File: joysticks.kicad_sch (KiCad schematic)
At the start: 20 parts, among them IC14 74HCT574, IC15 4HCT574

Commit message: prepare for fabrication
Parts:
- C104, C96: LCSC (none) -> C344201; LCSC Part (none) -> C344201
- IC14: LCSC (none) -> C6001; LCSC Part (none) -> C6001
- IC15: value 4HCT574 -> 74HCT574; LCSC (none) -> C6001; LCSC Part (none) -> C6001
- R100, R101, R106, R107, R108, R109, R98, R99: LCSC (none) -> C149504; LCSC Part (none) -> C149504
- R111, R112: LCSC (none) -> C2907326; LCSC Part (none) -> C2907326
- R225, R226: LCSC (none) -> C17630; LCSC Part (none) -> C17630
- RP1: value 10K -> 10Kx8; LCSC (none) -> C1738939; LCSC Part (none) -> C1738939
- RP10: value 4K7 -> 4K7x8; LCSC (none) -> C1739872; LCSC Part (none) -> C1739872

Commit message: move RP11 inline instead of pullup
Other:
- moved on the sheet: RP1A, RP1G, RP1H, RP1I, RP1J
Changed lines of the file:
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@@
 		(lib_name "R_Network15_Split_1")
 		(lib_id "Acorn:R_Network15_Split")
-		(at 124.46 3.81 0)
+		(at 271.78 19.05 0)
 		(unit 1)
 		(exclude_from_sim no)
@@
 		(fields_autoplaced yes)
 		(property "Reference" "RP1"
-			(at 127 3.1749 0)
+			(at 274.32 18.4149 0)
 			(effects
 				(font
@@
 		)
 		(property "Value" "10Kx8"
-			(at 127 5.08 0)
+			(at 274.32 20.32 0)
 			(effects
 				(font
@@
 		)
 		(property "Footprint" "Package_SO:SOIC-16W_5.3x10.2mm_P1.27mm"
-			(at 124.46 3.81 0)
+			(at 271.78 19.05 0)
 			(effects
 				(font
@@
 		)
 		(property "Datasheet" ""
-			(at 124.46 3.81 0)
+			(at 271.78 19.05 0)
 			(effects
 				(font
@@
 		)
 		(property "Description" ""
-			(at 124.46 3.81 0)
+			(at 271.78 19.05 0)
 			(effects
 				(font
@@
 		)
 		(property "LCSC" "C1738939"
-			(at 124.46 3.81 0)
+			(at 271.78 19.05 0)
 			(effects
 				(font
@@
 		)
 		(property "LCSC Part" "C1738939"
-			(at 124.46 3.81 0)
+			(at 271.78 19.05 0)
 			(effects
 				(font
@@
 		(lib_name "R_Network15_Split_3")
 		(lib_id "Acorn:R_Network15_Split")
-		(at 130.81 3.81 0)
+		(at 271.78 26.67 0)
 		(unit 7)
 		(exclude_from_sim no)
@@
 		(fields_autoplaced yes)
 		(property "Reference" "RP1"
-			(at 133.35 3.1749 0)
+			(at 274.32 26.0349 0)
 			(effects
 				(font
@@
 		)
 		(property "Value" "10Kx8"
-			(at 133.35 5.08 0)
+			(at 274.32 27.94 0)
 			(effects
 				(font
@@
 		)
 		(property "Footprint" "Package_SO:SOIC-16W_5.3x10.2mm_P1.27mm"
-			(at 130.81 3.81 0)
+			(at 271.78 26.67 0)
 			(effects
 				(font
@@
 		)
 		(property "Datasheet" ""
-			(at 130.81 3.81 0)
+			(at 271.78 26.67 0)
 			(effects
 				(font
@@
 		)
 		(property "Description" ""
-			(at 130.81 3.81 0)
+			(at 271.78 26.67 0)
 			(effects
 				(font
@@
 		)
 		(property "LCSC" "C1738939"
-			(at 130.81 3.81 0)
+			(at 271.78 26.67 0)
 			(effects
 				(font
@@
 		)
 		(property "LCSC Part" "C1738939"
-			(at 130.81 3.81 0)
+			(at 271.78 26.67 0)
 			(effects
 				(font
@@
 		(lib_name "R_Network15_Split_2")
 		(lib_id "Acorn:R_Network15_Split")
-		(at 135.89 3.81 0)
+		(at 271.78 34.29 0)
 		(unit 8)
 		(exclude_from_sim no)
@@
 		(fields_autoplaced yes)
 		(property "Reference" "RP1"
-			(at 138.43 3.1749 0)
+			(at 274.32 33.6549 0)
 			(effects
 				(font
@@
 		)
 		(property "Value" "10Kx8"
-			(at 138.43 5.08 0)
+			(at 274.32 35.56 0)
 			(effects
 				(font
@@
 		)
 		(property "Footprint" "Package_SO:SOIC-16W_5.3x10.2mm_P1.27mm"
-			(at 135.89 3.81 0)
+			(at 271.78 34.29 0)
 			(effects
 				(font
@@
 		)
 		(property "Datasheet" ""
-			(at 135.89 3.81 0)
+			(at 271.78 34.29 0)
 			(effects
 				(font
@@
 		)
 		(property "Description" ""
-			(at 135.89 3.81 0)
+			(at 271.78 34.29 0)
 			(effects
 				(font
@@
 		)
 		(property "LCSC" "C1738939"
-			(at 135.89 3.81 0)
+			(at 271.78 34.29 0)
 			(effects
 				(font
@@
 		)
 		(property "LCSC Part" "C1738939"
-			(at 135.89 3.81 0)
+			(at 271.78 34.29 0)
 			(effects
 				(font
@@
 		(lib_name "R_Network15_Split_5")
 		(lib_id "Acorn:R_Network15_Split")
-		(at 142.24 3.81 0)
+		(at 271.78 41.91 0)
 		(unit 9)
 		(exclude_from_sim no)
@@
 		(fields_autoplaced yes)
 		(property "Reference" "RP1"
-			(at 144.78 3.1749 0)
+			(at 274.32 41.2749 0)
 			(effects
 				(font
@@
 		)
 		(property "Value" "10Kx8"
-			(at 144.78 5.08 0)
+			(at 274.32 43.18 0)
 			(effects
 				(font
@@
 		)
 		(property "Footprint" "Package_SO:SOIC-16W_5.3x10.2mm_P1.27mm"
-			(at 142.24 3.81 0)
+			(at 271.78 41.91 0)
 			(effects
 				(font
@@
 		)
 		(property "Datasheet" ""
-			(at 142.24 3.81 0)
+			(at 271.78 41.91 0)
 			(effects
 				(font
@@
 		)
 		(property "Description" ""
-			(at 142.24 3.81 0)
+			(at 271.78 41.91 0)
 			(effects
 				(font
@@
 		)
 		(property "LCSC" "C1738939"
-			(at 142.24 3.81 0)
+			(at 271.78 41.91 0)
 			(effects
 				(font
@@
 		)
 		(property "LCSC Part" "C1738939"
-			(at 142.24 3.81 0)
+			(at 271.78 41.91 0)
 			(effects
 				(font
@@
 		(lib_name "R_Network15_Split_4")
 		(lib_id "Acorn:R_Network15_Split")
-		(at 148.59 3.81 0)
+		(at 271.78 49.53 0)
 		(unit 10)
 		(exclude_from_sim no)
@@
 		(fields_autoplaced yes)
 		(property "Reference" "RP1"
-			(at 151.13 3.1749 0)
+			(at 274.32 48.8949 0)
 			(effects
 				(font
@@
 		)
 		(property "Value" "10Kx8"
-			(at 151.13 5.08 0)
+			(at 274.32 50.8 0)
 			(effects
 				(font
@@
 		)
 		(property "Footprint" "Package_SO:SOIC-16W_5.3x10.2mm_P1.27mm"
-			(at 148.59 3.81 0)
+			(at 271.78 49.53 0)
 			(effects
 				(font
@@
 		)
 		(property "Datasheet" ""
-			(at 148.59 3.81 0)
+			(at 271.78 49.53 0)
 			(effects
 				(font
@@
 		)
 		(property "Description" ""
-			(at 148.59 3.81 0)
+			(at 271.78 49.53 0)
 			(effects
 				(font
@@
 		)
 		(property "LCSC" "C1738939"
-			(at 148.59 3.81 0)
+			(at 271.78 49.53 0)
 			(effects
 				(font
@@
 		)
 		(property "LCSC Part" "C1738939"
-			(at 148.59 3.81 0)
+			(at 271.78 49.53 0)
 			(effects
 				(font

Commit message: fix power domains
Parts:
- R108: value 100K -> 10K; LCSC C149504 -> C2907219; LCSC Part C149504 -> C2907219
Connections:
- net +5C: no longer R100.1, R101.1, R106.1, R107.1, R108.1, R109.1, R98.1, R99.1
- new net +5V: R100.1, R101.1, R106.1, R107.1, R108.1, R109.1, R98.1, R99.1
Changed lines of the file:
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@@
 	)
 	(junction
+		(at 31.75 29.21)
+		(diameter 0)
+		(color 0 0 0 0)
+	)
+	(junction
 		(at 50.8 63.5)
 		(diameter 0)
@@
 	)
 	(junction
-		(at 31.75 29.21)
-		(diameter 0)
-		(color 0 0 0 0)
-	)
-	(junction
 		(at 151.13 48.26)
 		(diameter 0)
@@
 			)
 		)
-		(property "Value" "100K"
+		(property "Value" "10K"
 			(at 28.194 40.894 0)
 			(effects
@@
 			)
 		)
-		(property "LCSC" "C149504"
+		(property "LCSC" "C2907219"
 			(at 34.29 39.37 0)
 			(effects
@@
 			)
 		)
-		(property "LCSC Part" "C149504"
+		(property "LCSC Part" "C2907219"
 			(at 34.29 39.37 0)
 			(effects
@@
 	)
 	(symbol
+		(lib_id "power:+5V")
+		(at 31.75 29.21 0)
+		(unit 1)
+		(exclude_from_sim no)
+		(in_bom yes)
+		(on_board yes)
+		(dnp no)
+		(fields_autoplaced yes)
+		(property "Reference" "#PWR032"
+			(at 31.75 33.02 0)
+			(effects
+				(font
+					(size 1.27 1.27)
+				)
+				(hide yes)
+			)
+		)
+		(property "Value" "+5V"
+			(at 31.75 24.13 0)
+			(effects
+				(font
+					(size 1.27 1.27)
+				)
+			)
+		)
+		(property "Footprint" ""
+			(at 31.75 29.21 0)
+			(effects
+				(font
+					(size 1.27 1.27)
+				)
+				(hide yes)
+			)
+		)
+		(property "Datasheet" ""
+			(at 31.75 29.21 0)
+			(effects
+				(font
+					(size 1.27 1.27)
+				)
+				(hide yes)
+			)
+		)
+		(property "Description" "Power symbol creates a global label with name \"+5V\""
+			(at 31.75 29.21 0)
+			(effects
+				(font
+					(size 1.27 1.27)
+				)
+				(hide yes)
+			)
+		)
+		(pin "1"
+		)
+		(instances
+			(project "Acorn-A3010"
+				(path "/999882f3-94f8-4a89-9093-27a47d0cb289/1d339b68-5722-4c6b-bdc7-0b741d7c0428"
+					(reference "#PWR032")
+					(unit 1)
+				)
+			)
+		)
+	)
+	(symbol
 		(lib_id "Device:C_Small")
 		(at 113.03 67.31 0)
@@
 				)
 			)
-		)
-	)
-	(symbol
-		(lib_id "power:+5C")
-		(at 31.75 29.21 0)
-		(unit 1)
-		(exclude_from_sim no)
-		(in_bom yes)
-		(on_board yes)
-		(dnp no)
-		(fields_autoplaced yes)
-		(property "Reference" "#PWR0292"
-			(at 31.75 33.02 0)
-			(effects
-				(font
-					(size 1.27 1.27)
-				)
-				(hide yes)
-			)
-		)
-		(property "Value" "+5C"
-			(at 31.75 24.13 0)
-			(effects
-				(font
-					(size 1.27 1.27)
-				)
-			)
-		)
-		(property "Footprint" ""
-			(at 31.75 29.21 0)
-			(effects
-				(font
-					(size 1.27 1.27)
-				)
-				(hide yes)
-			)
-		)
-		(property "Datasheet" ""
-			(at 31.75 29.21 0)
-			(effects
-				(font
-					(size 1.27 1.27)
-				)
-				(hide yes)
-			)
-		)
-		(property "Description" "Power symbol creates a global label with name \"+5C\""
-			(at 31.75 29.21 0)
-			(effects
-				(font
-					(size 1.27 1.27)
-				)
-				(hide yes)
-			)
-		)
-		(pin "1"
-		)
-		(instances
-			(project "Acorn-A3010"
-				(path "/999882f3-94f8-4a89-9093-27a47d0cb289/1d339b68-5722-4c6b-bdc7-0b741d7c0428"
-					(reference "#PWR0292")
-					(unit 1)
-				)
-			)

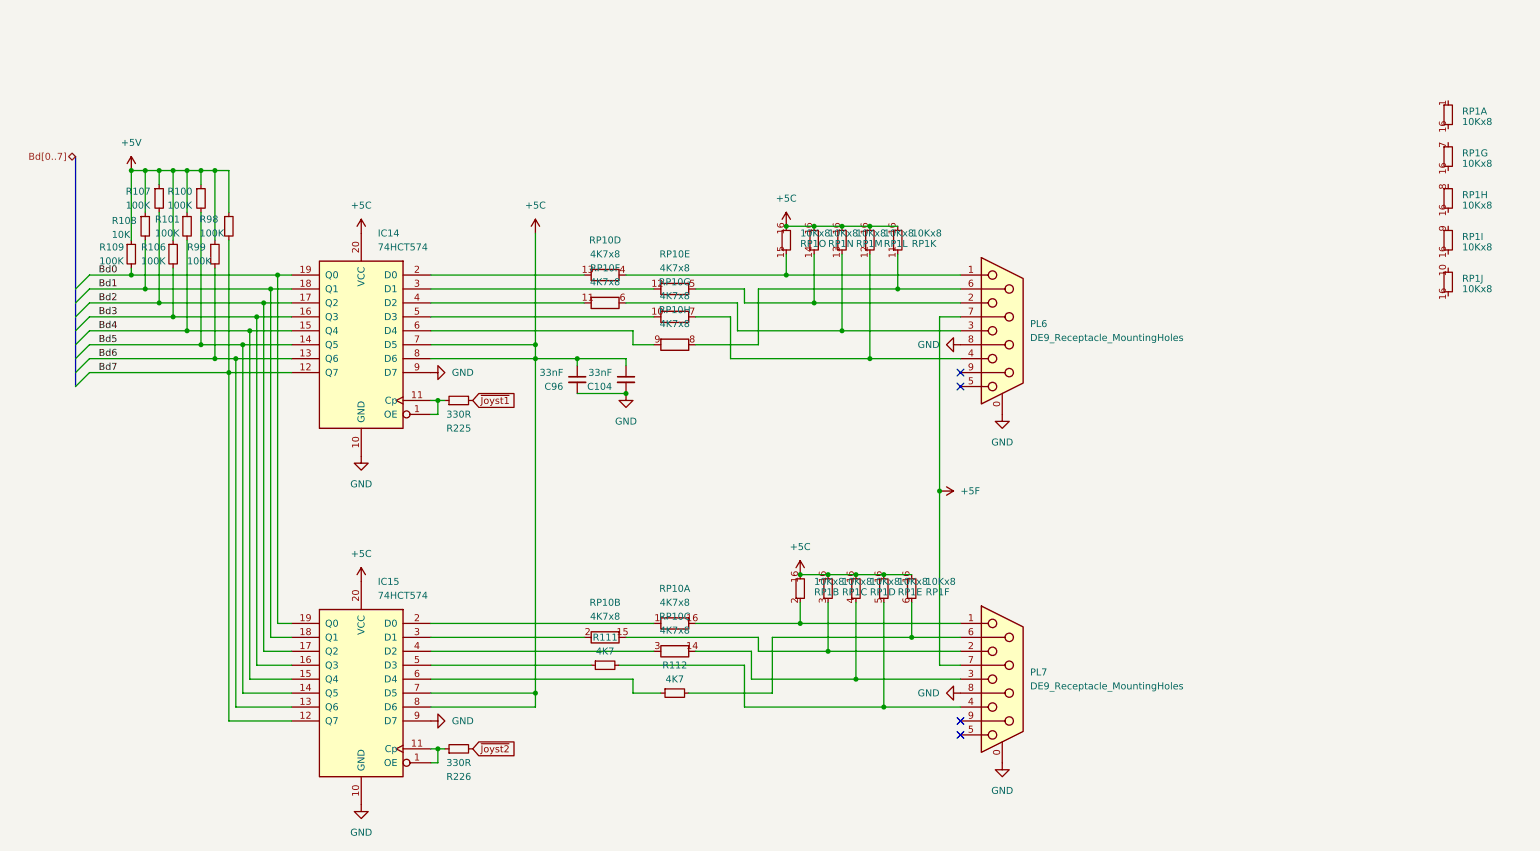
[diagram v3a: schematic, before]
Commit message: verify all component values vs TRM
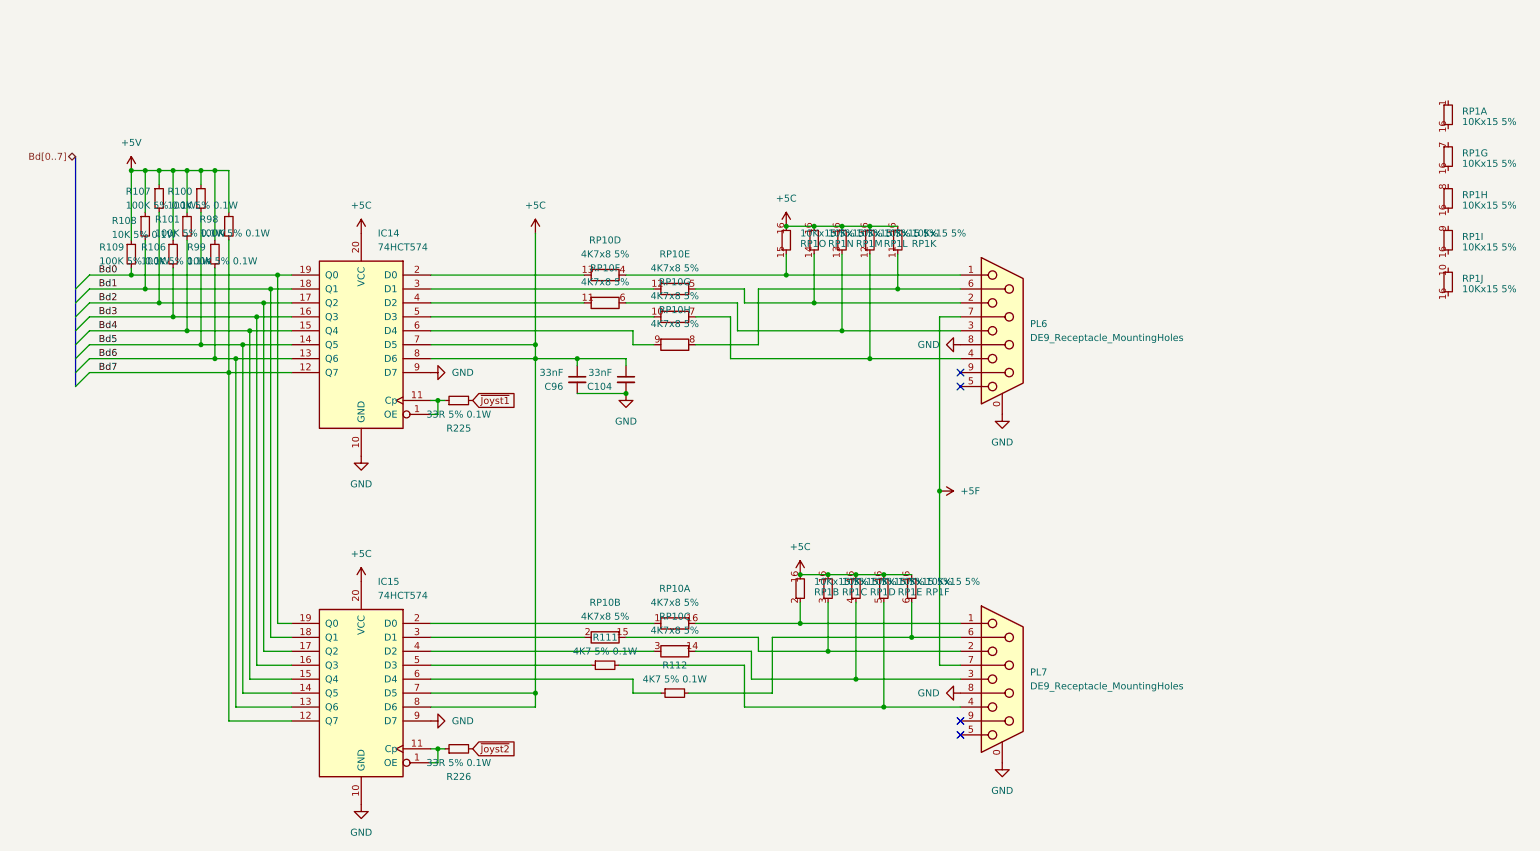
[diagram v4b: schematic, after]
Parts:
- R100, R101, R106, R107, R109, R98, R99: value 100K -> 100K 5% 0.1W
- R108: value 10K -> 10K 5% 0.1W
- R111, R112: value 4K7 -> 4K7 5% 0.1W
- R225, R226: value 330R -> 33R 5% 0.1W
- RP1: value 10Kx8 -> 10Kx15 5%
- RP10: value 4K7x8 -> 4K7x8 5%
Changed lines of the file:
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@@
 			)
 		)
-		(property "Value" "10Kx8"
+		(property "Value" "10Kx15 5%"
 			(at 173.99 40.64 0)
 			(effects
@@
 			)
 		)
-		(property "Value" "10Kx8"
+		(property "Value" "10Kx15 5%"
 			(at 166.37 104.14 0)
 			(effects
@@
 			)
 		)
-		(property "Value" "100K"
+		(property "Value" "100K 5% 0.1W"
 			(at 30.734 35.56 0)
 			(effects
@@
 			)
 		)
-		(property "Value" "10Kx8"
+		(property "Value" "10Kx15 5%"
 			(at 274.32 20.32 0)
 			(effects
@@
 			)
 		)
-		(property "Value" "4K7x8"
+		(property "Value" "4K7x8 5%"
 			(at 130.81 46.99 90)
 			(effects
@@
 			)
 		)
-		(property "Value" "10Kx8"
+		(property "Value" "10Kx15 5%"
 			(at 168.91 40.64 0)
 			(effects
@@
 			)
 		)
-		(property "Value" "10Kx8"
+		(property "Value" "10Kx15 5%"
 			(at 274.32 27.94 0)
 			(effects
@@
 			)
 		)
-		(property "Value" "10Kx8"
+		(property "Value" "10Kx15 5%"
 			(at 161.29 104.14 0)
 			(effects
@@
 			)
 		)
-		(property "Value" "4K7x8"
+		(property "Value" "4K7x8 5%"
 			(at 118.11 110.49 90)
 			(effects
@@
 			)
 		)
-		(property "Value" "4K7"
+		(property "Value" "4K7 5% 0.1W"
 			(at 130.81 121.92 90)
 			(effects
@@
 			)
 		)
-		(property "Value" "330R"
+		(property "Value" "33R 5% 0.1W"
 			(at 91.44 137.16 90)
 			(effects
@@
 			)
 		)
-		(property "Value" "10Kx8"
+		(property "Value" "10Kx15 5%"
 			(at 153.67 40.64 0)
 			(effects
@@
 			)
 		)
-		(property "Value" "4K7x8"
+		(property "Value" "4K7x8 5%"
 			(at 130.81 57.15 90)
 			(effects
@@
 			)
 		)
-		(property "Value" "10K"
+		(property "Value" "10K 5% 0.1W"
 			(at 28.194 40.894 0)
 			(effects
@@
 			)
 		)
-		(property "Value" "10Kx8"
+		(property "Value" "10Kx15 5%"
 			(at 176.53 104.14 0)
 			(effects
@@
 			)
 		)
-		(property "Value" "4K7x8"
+		(property "Value" "4K7x8 5%"
 			(at 130.81 107.95 90)
 			(effects
@@
 			)
 		)
-		(property "Value" "100K"
+		(property "Value" "100K 5% 0.1W"
 			(at 38.354 35.56 0)
 			(effects
@@
 			)
 		)
-		(property "Value" "10Kx8"
+		(property "Value" "10Kx15 5%"
 			(at 158.75 40.64 0)
 			(effects
@@
 			)
 		)
-		(property "Value" "4K7"
+		(property "Value" "4K7 5% 0.1W"
 			(at 118.11 116.84 90)
 			(effects
@@
 			)
 		)
-		(property "Value" "100K"
+		(property "Value" "100K 5% 0.1W"
 			(at 25.908 45.72 0)
 			(effects
@@
 			)
 		)
-		(property "Value" "4K7x8"
+		(property "Value" "4K7x8 5%"
 			(at 118.11 49.53 90)
 			(effects
@@
 			)
 		)
-		(property "Value" "100K"
+		(property "Value" "100K 5% 0.1W"
 			(at 44.196 40.64 0)
 			(effects
@@
 			)
 		)
-		(property "Value" "10Kx8"
+		(property "Value" "10Kx15 5%"
 			(at 156.21 104.14 0)
 			(effects
@@
 			)
 		)
-		(property "Value" "10Kx8"
+		(property "Value" "10Kx15 5%"
 			(at 171.45 104.14 0)
 			(effects
@@
 			)
 		)
-		(property "Value" "10Kx8"
+		(property "Value" "10Kx15 5%"
 			(at 274.32 35.56 0)
 			(effects
@@
 			)
 		)
-		(property "Value" "10Kx8"
+		(property "Value" "10Kx15 5%"
 			(at 274.32 43.18 0)
 			(effects
@@
 			)
 		)
-		(property "Value" "10Kx8"
+		(property "Value" "10Kx15 5%"
 			(at 163.83 40.64 0)
 			(effects
@@
 			)
 		)
-		(property "Value" "4K7x8"
+		(property "Value" "4K7x8 5%"
 			(at 130.81 52.07 90)
 			(effects
@@
 			)
 		)
-		(property "Value" "330R"
+		(property "Value" "33R 5% 0.1W"
 			(at 91.44 73.66 90)
 			(effects
@@
 			)
 		)
-		(property "Value" "4K7x8"
+		(property "Value" "4K7x8 5%"
 			(at 118.11 44.45 90)
 			(effects
@@
 			)
 		)
-		(property "Value" "100K"
+		(property "Value" "100K 5% 0.1W"
 			(at 36.068 40.64 0)
 			(effects
@@
 			)
 		)
-		(property "Value" "4K7x8"
+		(property "Value" "4K7x8 5%"
 			(at 130.81 113.03 90)
 			(effects
@@
 			)
 		)
-		(property "Value" "10Kx8"
+		(property "Value" "10Kx15 5%"
 			(at 274.32 50.8 0)
 			(effects
@@
 			)
 		)
-		(property "Value" "100K"
+		(property "Value" "100K 5% 0.1W"
 			(at 33.528 45.72 0)
 			(effects
@@
 			)
 		)
-		(property "Value" "100K"
+		(property "Value" "100K 5% 0.1W"
 			(at 41.91 45.72 0)
 			(effects
